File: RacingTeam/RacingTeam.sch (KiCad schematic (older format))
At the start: 68 parts, among them J1 BusIn, J2 PCB OUT, J3 Shutdown Circuit, J5 PreCharge Relay Out, J6 AIR, J7 AIR, J8 Precharge Relay, J9 Discharge Relay, Q1 2N7002, Q2 TP0610T, Q3 2N7002, Q4 TP0610T, Q5 TP0610T, Q6 2N7002, U1 LM311, U11 GLV-, U12 GLV+, U2 4N35, U3 NE555D, U4 GLV+, U5 GLV-, U6 GLV+, U6 LM311, U7 GLV-, U8 GLV-, U9 GLV-

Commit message: Update SPAN02A12.kicad_mod, EC3SAW.STEP, and 8 more files...
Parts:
- removed F1: 1000V 5A, symbol Device:Fuse
- removed J3: Shutdown Circuit, symbol Connector_Generic:Conn_01x02
- removed J8: Precharge Relay, symbol Connector_Generic:Conn_01x02
- removed J9: Discharge Relay, symbol Connector_Generic:Conn_01x02
- removed PS1: SPAN02A-12, Footprints:SPAN02A12, symbol RacingTeamPCB:SPAN02A-12
- removed R24: 2kΩ, Footprints:R_0603_1608Metric, symbol RacingTeamPCB:R
- removed R?: 100Ω, Footprints:R_0603_1608Metric, symbol RacingTeamPCB:R
- added D4, D5, D6: Flyback, symbol Device:D
- added D7: 12V, symbol RacingTeamPCB:D_Zener
- added D7: LED, symbol RacingTeamPCB:LED
- added J3, J4, J8, J9: Conn_01x01, symbol Connector_Generic:Conn_01x01
- added PS1: EC3SAW-24S12P, symbol RacingTeamPCB:EC3SAW-24S12P
- added Q7, Q8: 2N7002, symbol RacingTeamPCB:2N7000
- added R13: 1.2kΩ, symbol RacingTeamPCB:R
- added R18: 22kΩ, symbol RacingTeamPCB:R
- added R28, R29, R30: 0Ω, symbol RacingTeamPCB:R
- added U10: GLV-, symbol RacingTeamPCB:GLV-
- C1, C2, C3, C4, C5, C6, C7, C8: footprint Footprints:C_0603_1608Metric -> (none)
- J6: value AIR -> AIROut
- J7: value AIR -> Discharge Relay Out
- Q1, Q2, Q3, Q4, Q5, Q6: footprint Package_TO_SOT_SMD:SOT-23 -> (none)
- R1, R10, R11, R2, R3, R4, R5, R6, R7, R8, R9: footprint Footprints:R_0603_1608Metric -> (none)
- R12, R25: renamed from R23; footprint Footprints:R_0603_1608Metric -> (none)
- R14: renamed from R12; footprint Footprints:R_0603_1608Metric -> (none)
- R15: renamed from R13; footprint Footprints:R_0603_1608Metric -> (none)
- R16: renamed from R14; footprint Footprints:R_0603_1608Metric -> (none)
- R17: renamed from R15; footprint Footprints:R_0603_1608Metric -> (none)
- R19: renamed from R16; footprint Footprints:R_0603_1608Metric -> (none)
- R20: renamed from R17; footprint Footprints:R_0603_1608Metric -> (none)
- R21: renamed from R20; footprint Footprints:R_0603_1608Metric -> (none)
- R22: renamed from R21; footprint Footprints:R_0603_1608Metric -> (none)
- R23: renamed from R18; footprint Footprints:R_0603_1608Metric -> (none)
- R24: renamed from R19; footprint Footprints:R_0603_1608Metric -> (none)
- R26: renamed from R24; footprint Footprints:R_0603_1608Metric -> (none)
- R27: renamed from R22; footprint Footprints:R_0603_1608Metric -> (none)
- U1: footprint Footprints:TSSOP-8 -> (none)
- U2: footprint Footprints:4N35PDIP-SMD -> (none)
- U3: footprint Footprints:SOIC-8_3.9x4.9mm_P1.27mm -> (none)
- gave numbers to parts that had none: 2
- renumbered U6 to U20
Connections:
- net labels added: AIROR, PreChargeOR
- net labels removed: Discharge+, Discharge-, PrechargeIn
- wire segments 165 -> 173
- no-connect marks 4 -> 3
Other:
- note added: "12V+ - Unconverted 12V from Battery\nVCC - Diode Filtered GLV+\nGLV+ - Grounded Low Voltage +\nGLV- - Grounded Low Voltage -"
- note added: "Discharge Control\n"
- note added: "Drain\nGate\nSource"
- note added: "If=10mA"
- note added: "PreCharge Control\n\n"
- note added: "Source\nGate\nDrain\n"
- note removed: "Discharge"
- note removed: "Logic\n1. Shutdown Circuit Open Car On = Precharge Relay Open\n2. Shutdown Circuit Open Car Off = Precharge Relay Open\n3. Shutdown Circuit Closed Car Off = Precharge Relay Open\n4. Shutdown Circuit Closed Car On = Precharge Relay Closed"
- note removed: "PreCharge and Discharge (Control Side)\n"
- note removed: "Precharge and Discharge Relay (Drive Side)\n"
- note removed: "Shutdown Initiation"
- moved on the sheet: D3, J2, J5, J6, Q5, Q6

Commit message: Update RacingTeam.zip, PCBBom.xlsx, and 2 more files...
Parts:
- added R22, R23: 150kOhm, symbol Device:R
- R21: value 105kOhm -> 150kOhm
- R24: renamed from R22; value 1kOhm -> 4kOhm
- renumbered R23 to R25, R24 to R26, R25 to R27, R26 to R28, R27 to R29
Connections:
- net at D7.1 (K), J8.1 (Pin_1), R24.1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: now also R23.2; no longer R21.2
- new net: R21.2, R22.1
- new net: R22.2, R23.1
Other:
- moved on the sheet: C7, C8, D4, D5, D7, J5, J6, J8, J9, Q5, Q6, R21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

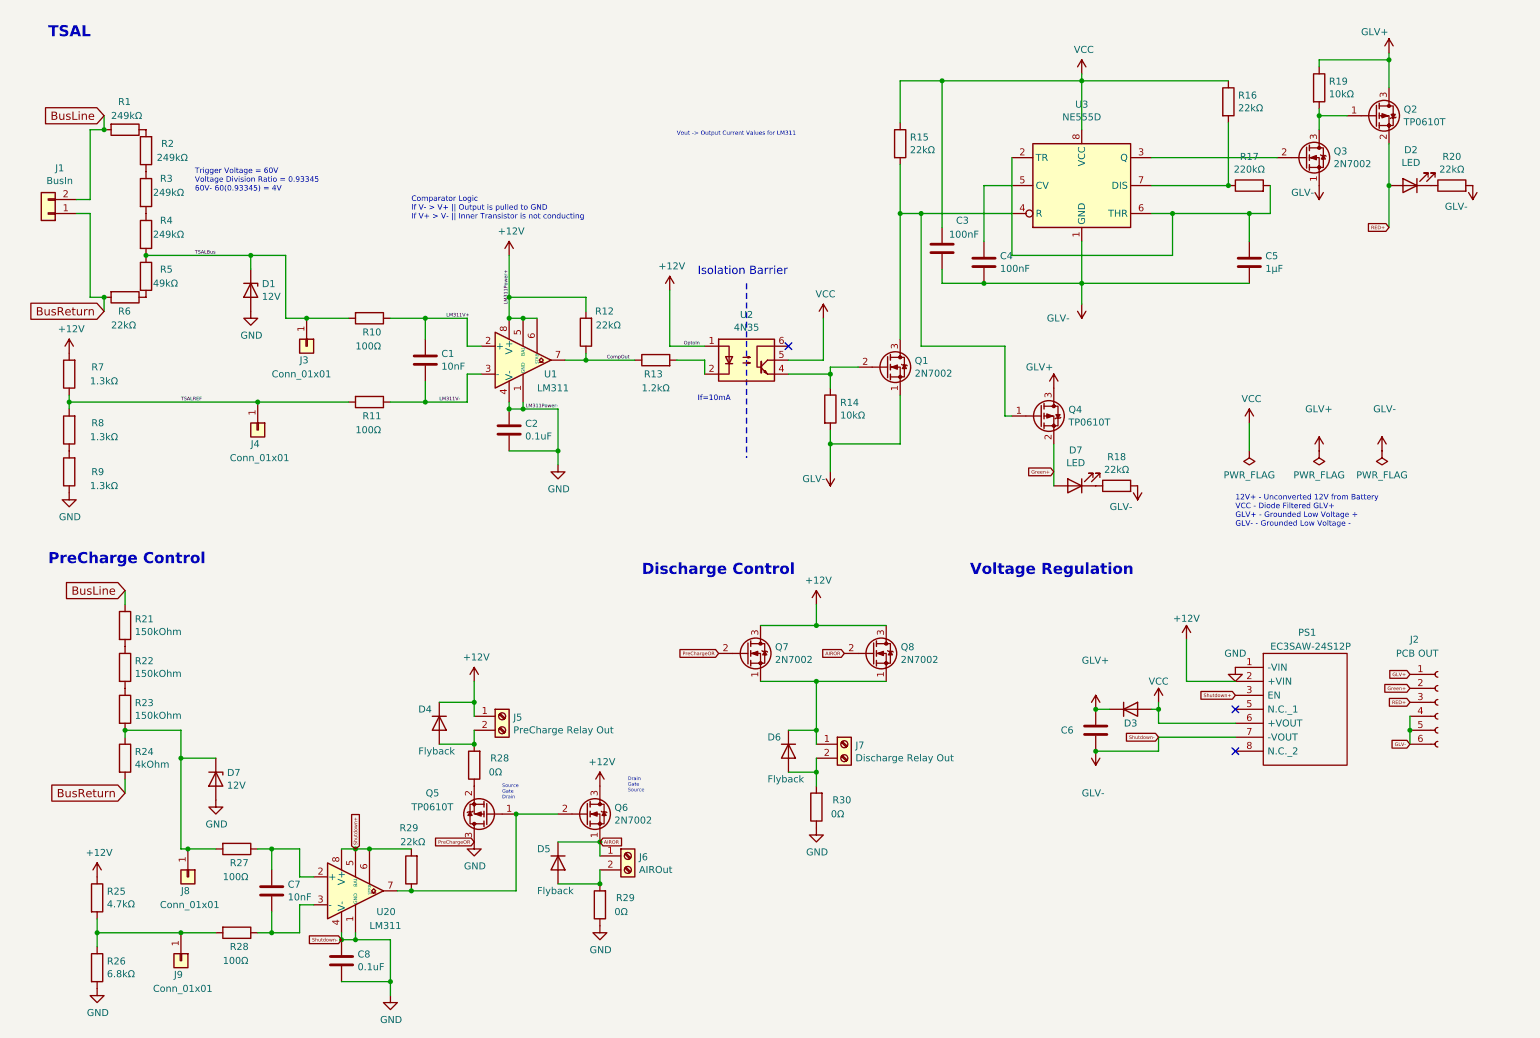
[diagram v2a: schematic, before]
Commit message: Update 2N7002H6327XTSA2.kicad_mod, 4N35SM.kicad_mod, and 21 more files...
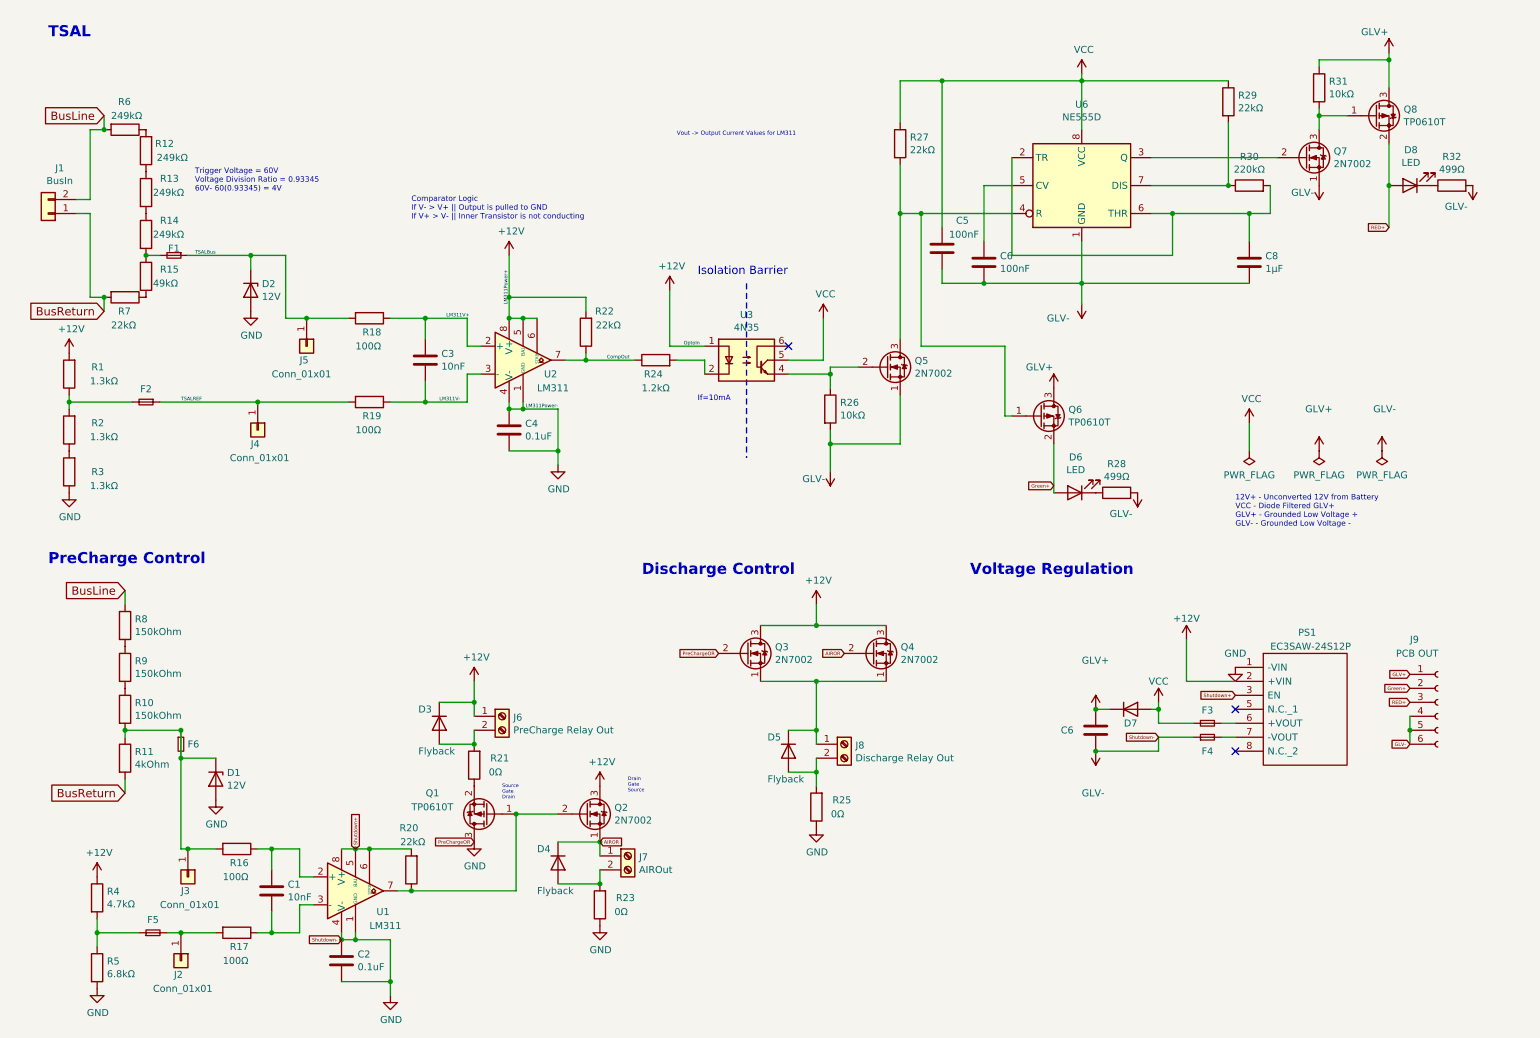
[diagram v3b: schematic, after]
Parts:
- added F1, F2, F3, F4, F5, F6: Fuse_Small, symbol Device:Fuse_Small
- C1: renamed from C7; footprint (none) -> GRC2022:C_0603
- C2: renamed from C8; footprint (none) -> GRC2022:C_0603
- C3: renamed from C1; footprint (none) -> GRC2022:C_0603
- C4: renamed from C2; footprint (none) -> GRC2022:C_0603
- C5: renamed from C3; footprint (none) -> GRC2022:C_0603
- C6: renamed from C4; footprint (none) -> GRC2022:C_0603
- C7: renamed from C6; footprint (none) -> GRC2022:C_0603
- C8: renamed from C5; footprint (none) -> GRC2022:C_0603
- D1: renamed from D7; footprint (none) -> GRC2022:SOD57-10
- D2: renamed from D1; footprint (none) -> GRC2022:SOD57-10
- D3: renamed from D4; footprint (none) -> GRC2022:SD0805S040S0R5
- D4: renamed from D5; footprint (none) -> GRC2022:SD0805S040S0R5
- D5: renamed from D6; footprint (none) -> GRC2022:SD0805S040S0R5
- D6: renamed from D7; footprint (none) -> GRC2022:SunLED
- D7: renamed from D3; footprint (none) -> GRC2022:SD0805S040S0R5
- D8: renamed from D2; footprint (none) -> GRC2022:SunLED
- J1: footprint (none) -> GRC2022:TE_8PCV-02-006
- J2: renamed from J9; footprint (none) -> GRC2022:SinglePinHeader
- J3: renamed from J8; footprint (none) -> GRC2022:SinglePinHeader
- J4: footprint (none) -> GRC2022:SinglePinHeader
- J5: renamed from J3; footprint (none) -> GRC2022:SinglePinHeader
- J6: renamed from J5; footprint (none) -> GRC2022:CUI_TBL001-500-02GY-2GY
- J7: renamed from J6; footprint (none) -> GRC2022:CUI_TBL001-500-02GY-2GY
- J8: renamed from J7; footprint (none) -> GRC2022:CUI_TBL001-500-02GY-2GY
- J9: renamed from J2; footprint (none) -> GRC2022:Molex
- PS1: footprint (none) -> GRC2022:EC3SAW-24S12P
- Q1: renamed from Q5; footprint (none) -> GRC2022:SOT95P280X100-6N
- Q2: renamed from Q6; footprint (none) -> GRC2022:TRANS_MMBT2907A
- Q3: renamed from Q7; footprint (none) -> GRC2022:TRANS_MMBT2907A
- Q4: renamed from Q8; footprint (none) -> GRC2022:TRANS_MMBT2907A
- Q5: renamed from Q1; footprint (none) -> GRC2022:TRANS_MMBT2907A
- Q6: renamed from Q4; footprint (none) -> GRC2022:SOT95P280X100-6N
- Q7: renamed from Q3; footprint (none) -> GRC2022:SOP65P640X120-8N
- Q8: renamed from Q2; footprint (none) -> GRC2022:SOT95P280X100-6N
- R1: renamed from R7; footprint (none) -> GRC2022:R_0603
- R10: renamed from R23; footprint (none) -> GRC2022:R_0805
- R11: renamed from R24; footprint (none) -> GRC2022:R_0805
- R12: renamed from R2; footprint (none) -> GRC2022:R_0805
- R13: renamed from R3; footprint (none) -> GRC2022:R_0805
- R14: renamed from R4; footprint (none) -> GRC2022:R_0805
- R15: renamed from R5; footprint (none) -> GRC2022:R_0805
- R16: renamed from R27; footprint (none) -> GRC2022:R_0603
- R17, R21: renamed from R28; footprint (none) -> GRC2022:R_0603
- R18: renamed from R10; footprint (none) -> GRC2022:R_0603
- R19: renamed from R11; footprint (none) -> GRC2022:R_0603
- R2: renamed from R8; footprint (none) -> GRC2022:R_0603
- R20, R23: renamed from R29; footprint (none) -> GRC2022:R_0603
- R22: renamed from R12; footprint (none) -> GRC2022:R_0603
- R24: renamed from R13; footprint (none) -> GRC2022:R_0603
- R25: renamed from R30; footprint (none) -> GRC2022:R_0603
- R26: renamed from R14; footprint (none) -> GRC2022:R_0603
- R27: renamed from R15; footprint (none) -> GRC2022:R_0603
- R28: renamed from R18; value 22kΩ -> 499Ω; footprint (none) -> GRC2022:R_0603
- R29: renamed from R16; footprint (none) -> GRC2022:R_0603
- R3: renamed from R9; footprint (none) -> GRC2022:R_0603
- R30: renamed from R17; footprint (none) -> GRC2022:R_0603
- R31: renamed from R19; footprint (none) -> GRC2022:R_0603
- R32: renamed from R20; value 22kΩ -> 499Ω; footprint (none) -> GRC2022:R_0603
- R4: renamed from R25; footprint (none) -> GRC2022:R_0603
- R5: renamed from R26; footprint (none) -> GRC2022:R_0603
- R6: renamed from R1; footprint (none) -> GRC2022:R_0805
- R7: renamed from R6; footprint (none) -> GRC2022:R_0603
- R8: renamed from R21; footprint (none) -> GRC2022:R_0805
- R9: renamed from R22; footprint (none) -> GRC2022:R_0805
- U1: renamed from U20; footprint (none) -> GRC2022:SOP65P640X120-8N
- U2: renamed from U1; footprint (none) -> GRC2022:SOP65P640X120-8N
- U3: renamed from U2; footprint (none) -> GRC2022:OPTO_4N35SM
- U6: renamed from U3; footprint (none) -> GRC2022:NE555PSRE4
- renumbered U8 to U11, U13 to U12, U14 to U13, U12 to U14, U9 to U15, U11 to U4, U4 to U5, U5 to U7, U6 to U8, U7 to U9
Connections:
- net GLV-: now also F4.1; no longer PS1.7 (-VOUT)
- net TSALBus: now also F1.1; no longer R14.2, R15.1
- net TSALREF: now also F2.1; no longer R1.1, R2.2
- net VCC: now also F3.1; no longer PS1.6 (+VOUT)
- net at R4.2, R5.1: now also F5.1; no longer J2.1 (Pin_1), R17.2
- net at D1.1 (K), J3.1 (Pin_1), R10.2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: now also F6.1, F6.2
- new net: F1.2, R14.2, R15.1
- new net: F2.2, R1.1, R2.2
- new net: F5.2, J2.1 (Pin_1), R17.2
- new net: F3.2, PS1.6 (+VOUT)
- new net: F4.2, PS1.7 (-VOUT)
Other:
- moved on the sheet: D6, R28

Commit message: Update FUSE_0154004.DRTL.kicad_mod, GRC2022.mod, and 15 more files...
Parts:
- removed C7: C6, GRC2022:C_0603, symbol RacingTeamPCB:C
- removed F4: Fuse_Small, symbol Device:Fuse_Small
- removed U10, U11, U13, U15, U4, U7, U9: GLV-, symbol RacingTeamPCB:GLV-
- removed U12, U14, U5, U8: GLV+, symbol RacingTeamPCB:GLV+
- added JP1, JP2: Jumper, GRC2022:DualPinHeader, symbol RacingTeamPCB:Jumper
- F1, F2, F3, F5, F6: footprint (none) -> GRC2022:FUSE_0154004.DRTL
- J9: symbol RacingTeamPCB:Conn_01x06_Female -> RacingTeamPCB:Conn_01x06
- Q7: footprint GRC2022:SOP65P640X120-8N -> GRC2022:TRANS_MMBT2907A
- R7: footprint GRC2022:R_0603 -> GRC2022:R_0805
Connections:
- net BusLine: now also J1.1 (Pin_1); no longer J1.2 (Pin_2)
- net BusReturn: now also J1.2 (Pin_2); no longer J1.1 (Pin_1)
- net GLV-: now also PS1.7 (-VOUT); no longer C2.1, C2.2, C4.1, C4.2, D1.2 (A), D2.2 (A), PS1.1 (-VIN), Q1.3 (D), Q3.2 (G), R23.1, R25.1, R3.1, R5.2, U1.1 (GND), U1.4 (V-), U2.1 (GND), U2.4 (V-)
- net Green+: now also JP1.1; no longer D6.2 (A)
- net RED+: now also JP2.1; no longer D8.2 (A)
- net Shutdown+: no longer R20.2, U1.5 (BAL), U1.6 (STRB), U1.8 (V+)
- net PreChargeV+: now reaches C1.1, R16.1, U1.2 (+)
- net PrechargeV-: now reaches C1.2, R17.1, U1.3 (-)
- net PrechargeOUT: now reaches Q1.1 (G), Q2.2 (G), R20.1, U1.7
- net PrechargeRef: now reaches F5.1, R4.2, R5.1
- net PrechargeTP+: now reaches D1.1 (K), F6.1, F6.2, J3.1 (Pin_1), R10.2, R11.1, R16.2
- net PreChargeOn: now reaches Q1.2 (S), R21.1
- net PreChargeOn: now also Q3.2 (G)
- net PrechargeTP-: now reaches F5.2, J2.1 (Pin_1), R17.2
- net AIROR renamed AIROn
- new net: D8.2 (A), JP2.2
- new net: D6.2 (A), JP1.2
- new net GND: C2.1, C2.2, C4.1, C4.2, D1.2 (A), D2.2 (A), PS1.1 (-VIN), Q1.3 (D), R23.1, R25.1, R3.1, R5.2, U1.1 (GND), U1.4 (V-), U2.1 (GND), U2.4 (V-)
- new net PreChargePullup: R20.2, U1.5 (BAL), U1.6 (STRB), U1.8 (V+)
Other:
- moved on the sheet: D6, D7, D8, F3, PS1, R28, R32

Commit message: Update FSAELogo.kicad_mod, GRC2022.mod, and 11 more files...
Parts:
- added J10: BatteryIn, GRC2022:CUI_TBL001-500-02GY-2GY, symbol Connector:Screw_Terminal_01x02
- added J11: ShutdownIn, GRC2022:CUI_TBL001-500-02GY-2GY, symbol Connector:Screw_Terminal_01x02
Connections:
- net +12V: now also J10.1 (Pin_1)
- net GLV-: now also J11.2 (Pin_2)
- net GND: now also J10.2 (Pin_2)
- net Shutdown+: now also J11.1 (Pin_1)
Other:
- note added: "ConnectorsIn\n\n"
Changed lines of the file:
@@
 L power:PWR_FLAG #FLG03
 U 1 1 624032E8
-P 10750 3650
-F 0 "#FLG03" H 10750 3725 50  0001 C CNN
-F 1 "PWR_FLAG" H 10750 3823 50  0000 C CNN
-F 2 "" H 10750 3650 50  0001 C CNN
-F 3 "~" H 10750 3650 50  0001 C CNN
-	1    10750 3650
+P 3900 1000
+F 0 "#FLG03" H 3900 1075 50  0001 C CNN
+F 1 "PWR_FLAG" H 3900 1173 50  0000 C CNN
+F 2 "" H 3900 1000 50  0001 C CNN
+F 3 "~" H 3900 1000 50  0001 C CNN
+	1    3900 1000
 	-1   0    0    1
 $EndComp
@@
 L power:PWR_FLAG #FLG02
 U 1 1 6240499A
-P 10300 3650
-F 0 "#FLG02" H 10300 3725 50  0001 C CNN
-F 1 "PWR_FLAG" H 10300 3823 50  0000 C CNN
-F 2 "" H 10300 3650 50  0001 C CNN
-F 3 "~" H 10300 3650 50  0001 C CNN
-	1    10300 3650
+P 3450 1000
+F 0 "#FLG02" H 3450 1075 50  0001 C CNN
+F 1 "PWR_FLAG" H 3450 1173 50  0000 C CNN
+F 2 "" H 3450 1000 50  0001 C CNN
+F 3 "~" H 3450 1000 50  0001 C CNN
+	1    3450 1000
 	-1   0    0    1
 $EndComp
@@
 L RacingTeamPCB:GLV- #U013
 U 1 1 62404C8F
-P 10750 3600
-F 0 "#U013" H 10672 3554 50  0001 R CNN
-F 1 "GLV-" H 10850 3300 50  0000 R CNN
-F 2 "" H 10750 3600 50  0001 C CNN
-F 3 "" H 10750 3600 50  0001 C CNN
-	1    10750 3600
+P 3900 950
+F 0 "#U013" H 3822 904 50  0001 R CNN
+F 1 "GLV-" H 4000 650 50  0000 R CNN
+F 2 "" H 3900 950 50  0001 C CNN
+F 3 "" H 3900 950 50  0001 C CNN
+	1    3900 950
 	-1   0    0    1
 $EndComp
@@
 L RacingTeamPCB:GLV+ #U012
 U 1 1 62407966
-P 10300 3600
-F 0 "#U012" H 10378 3638 50  0001 L CNN
-F 1 "GLV+" H 10200 3900 50  0000 L CNN
-F 2 "" H 10300 3600 50  0001 C CNN
-F 3 "" H 10300 3600 50  0001 C CNN
-	1    10300 3600
+P 3450 950
+F 0 "#U012" H 3528 988 50  0001 L CNN
+F 1 "GLV+" H 3350 1250 50  0000 L CNN
+F 2 "" H 3450 950 50  0001 C CNN
+F 3 "" H 3450 950 50  0001 C CNN
+	1    3450 950
 	1    0    0    -1
 $EndComp
@@
 L power:PWR_FLAG #FLG01
 U 1 1 6241A99A
-P 9800 3650
-F 0 "#FLG01" H 9800 3725 50  0001 C CNN
-F 1 "PWR_FLAG" H 9800 3823 50  0000 C CNN
-F 2 "" H 9800 3650 50  0001 C CNN
-F 3 "~" H 9800 3650 50  0001 C CNN
-	1    9800 3650
+P 2950 1000
+F 0 "#FLG01" H 2950 1075 50  0001 C CNN
+F 1 "PWR_FLAG" H 2950 1173 50  0000 C CNN
+F 2 "" H 2950 1000 50  0001 C CNN
+F 3 "~" H 2950 1000 50  0001 C CNN
+	1    2950 1000
 	-1   0    0    1
 $EndComp
@@
 L power:VCC #PWR022
 U 1 1 6241ADD0
-P 9800 3600
-F 0 "#PWR022" H 9800 3450 50  0001 C CNN
-F 1 "VCC" H 9800 3900 50  0000 C CNN
-F 2 "" H 9800 3600 50  0001 C CNN
-F 3 "" H 9800 3600 50  0001 C CNN
-	1    9800 3600
+P 2950 950
+F 0 "#PWR022" H 2950 800 50  0001 C CNN
+F 1 "VCC" H 2950 1250 50  0000 C CNN
+F 2 "" H 2950 950 50  0001 C CNN
+F 3 "" H 2950 950 50  0001 C CNN
+	1    2950 950
 	1    0    0    -1
 $EndComp
@@
 Wire Wire Line
 	8850 5750 9200 5750
-Text Notes 9700 4200 0    39   ~ 0
+Text Notes 2850 1550 0    39   ~ 0
 12V+ - Unconverted 12V from Battery\nVCC - Diode Filtered GLV+\nGLV+ - Grounded Low Voltage +\nGLV- - Grounded Low Voltage -
 Wire Wire Line
@@
 $EndComp
 Wire Wire Line
-	10300 3600 10300 3650
+	3450 950  3450 1000
 Wire Wire Line
-	10750 3600 10750 3650
+	3900 950  3900 1000
 Wire Wire Line
-	9800 3600 9800 3650
+	2950 950  2950 1000
 $Comp
 L RacingTeamPCB:2N7000 Q7
@@
 Wire Wire Line
 	8200 6250 8650 6250
+Text Label 8250 5950 0    25   ~ 0
+GLV+
+$Comp
+L Connector:Screw_Terminal_01x02 J10
+U 1 1 624243D7
+P 9850 3550
+F 0 "J10" H 9930 3542 50  0000 L CNN
+F 1 "BatteryIn" H 9930 3451 50  0000 L CNN
+F 2 "GRC2022:CUI_TBL001-500-02GY-2GY" H 9850 3550 50  0001 C CNN
+F 3 "~" H 9850 3550 50  0001 C CNN
+	1    9850 3550
+	1    0    0    -1
+$EndComp
+$Comp
+L power:+12V #PWR0101
+U 1 1 6242E315
+P 9650 3550
+F 0 "#PWR0101" H 9650 3400 50  0001 C CNN
+F 1 "+12V" H 9665 3723 50  0000 C CNN
+F 2 "" H 9650 3550 50  0001 C CNN
+F 3 "" H 9650 3550 50  0001 C CNN
+	1    9650 3550
+	1    0    0    -1
+$EndComp
+$Comp
+L power:GND #PWR0102
+U 1 1 6242F490
+P 9650 3650
+F 0 "#PWR0102" H 9650 3400 50  0001 C CNN
+F 1 "GND" H 9655 3477 50  0000 C CNN
+F 2 "" H 9650 3650 50  0001 C CNN
+F 3 "" H 9650 3650 50  0001 C CNN
+	1    9650 3650
+	1    0    0    -1
+$EndComp
+$Comp
+L Connector:Screw_Terminal_01x02 J11
+U 1 1 62430F4E
+P 10050 4150
+F 0 "J11" H 10130 4142 50  0000 L CNN
+F 1 "ShutdownIn" H 10130 4051 50  0000 L CNN
+F 2 "GRC2022:CUI_TBL001-500-02GY-2GY" H 10050 4150 50  0001 C CNN
+F 3 "~" H 10050 4150 50  0001 C CNN
+	1    10050 4150
+	1    0    0    -1
+$EndComp
+Text GLabel 9850 4150 0    25   Input ~ 0
+Shutdown+
+Text GLabel 9850 4250 0    25   Input ~ 0
+Shutdown-
+Text Notes 8700 3450 0    79   ~ 16
+ConnectorsIn\n\n
 Text GLabel 8650 6150 0    25   Input ~ 0
 Shutdown-
